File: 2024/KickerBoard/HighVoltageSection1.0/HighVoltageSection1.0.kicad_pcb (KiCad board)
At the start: 2 copper layers, 59.8 x 28.9 mm, 17 parts, among them J10 Conn_01x02_Socket, J3 Conn_01x02_Socket, J4 Conn_01x02_Socket, J6 Conn_01x02_Socket, J7 Conn_01x02_Socket, J8 Conn_01x04_Socket, J9 Conn_01x04_Socket, Q2 NMOS, Q3 NMOS

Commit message: add Kick&Sub
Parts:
- J3, J4, J6, J7: footprint Connector_AMASS:AMASS_XT30UPB-F_1x02_P5.0mm_Vertical -> Connector_Molex:Molex_SPOX_5267-02A_1x02_P2.50mm_Vertical
- moved J3 125.3 mm to (-29.6, -8.27)
- moved J6 113.2 mm to (-23.8, 10.4)
- moved Q3 111.7 mm to (24.7, -5.62)
- moved J10 111.1 mm to (-5.00, -1.00)
- moved C8 110.3 mm to (-8.63, -7.63)
- moved D3 110.3 mm to (21.1, 0.60)
- moved G*** 110.3 mm to (2.00, -5.87)
- moved J9 110.3 mm to (17.3, -12.1)
- moved R10 110.3 mm to (21.8, -4.22)
- moved R11 110.3 mm to (21.8, -6.51)
- moved J7 108.7 mm to (22.6, 9.50)
- moved J8 108.6 mm to (-20.1, -11.8)
- moved Q2 107.2 mm to (-24.7, -5.62)
- moved R9 106.9 mm to (-20.4, -5.67)
- moved R8 106.5 mm to (-20.2, -2.87)
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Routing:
- net CHIP: track 51.0 -> 27.4 mm
- net STRAIGHT: track 23.0 -> 12.6 mm
- net GATE1: track 0.00 -> 3.10 mm
- net VOUT: vias 37 -> 27
- net OUTGND2: vias 8 -> 6
- net OUTGND1: vias 7 -> 5
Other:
- board size 59.8 x 28.9 mm -> 66 x 27.4 mm

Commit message: add Kick&Sub
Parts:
- removed J10: Conn_01x02_Socket, Connector_PinHeader_2.54mm:PinHeader_1x02_P2.54mm_Vertical
- removed J8, J9: Conn_01x04_Socket, Connector_PinHeader_2.54mm:PinHeader_2x02_P2.54mm_Vertical
- added J2: Conn_01x02_Socket, Connector_PinHeader_2.54mm:PinHeader_1x02_P2.54mm_Vertical, F.Cu at (-5.00, -0.12)
- added J3: Conn_01x02_Socket, Connector_PinHeader_2.54mm:PinHeader_1x02_P2.54mm_Vertical, F.Cu at (-20.0, -9.00)
- added J4: Conn_01x02_Socket, Connector_PinHeader_2.54mm:PinHeader_1x02_P2.54mm_Vertical, F.Cu at (20.0, -9.00)
- moved G*** 9.00 mm to (11.0, -6.00)
- moved Q2 6.58 mm to (-30.5, -2.50)
- moved Q3 6.47 mm to (30.5, -2.75)
- moved C8 6.04 mm to (-13.9, -10.5)
- moved J4 5.31 mm to (25.5, -8.00)
- moved R9 4.89 mm to (-25.0, -4.00)
- moved R8 4.88 mm to (-25.0, -2.00)
- moved J3 4.67 mm to (-25.5, -10.5), turned to -90 degrees
- moved D2 4.40 mm to (-22.0, 2.00)
- moved R11 4.03 mm to (25.0, -4.00)
- moved R10 3.86 mm to (25.0, -2.00)
- moved D3 1.64 mm to (22.0, 2.00)
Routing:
- net STRAIGHT: track 12.6 -> 17.4 mm
- net GATE1: track 3.10 -> 0.00 mm
- net CHIP: track 27.4 -> 30.0 mm
- net VOUT: vias 27 -> 7
- net OUTGND2: vias 6 -> 1
- net OUTGND1: vias 5 -> 1
- net GNDPWR: vias 35 -> 25
- added copper zone on F.Cu, net GATE1
- added copper zone on F.Cu, net GATE2

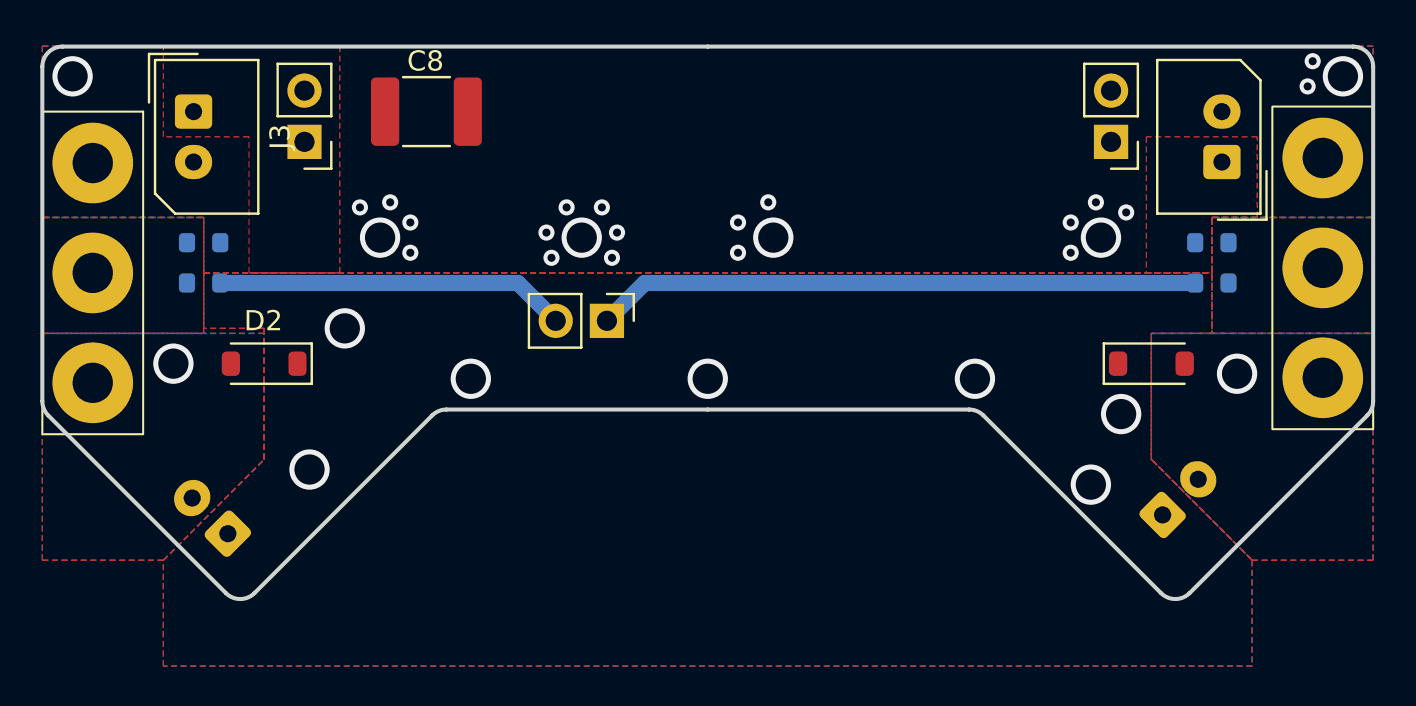
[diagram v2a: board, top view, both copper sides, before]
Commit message: add Sub&dcdc
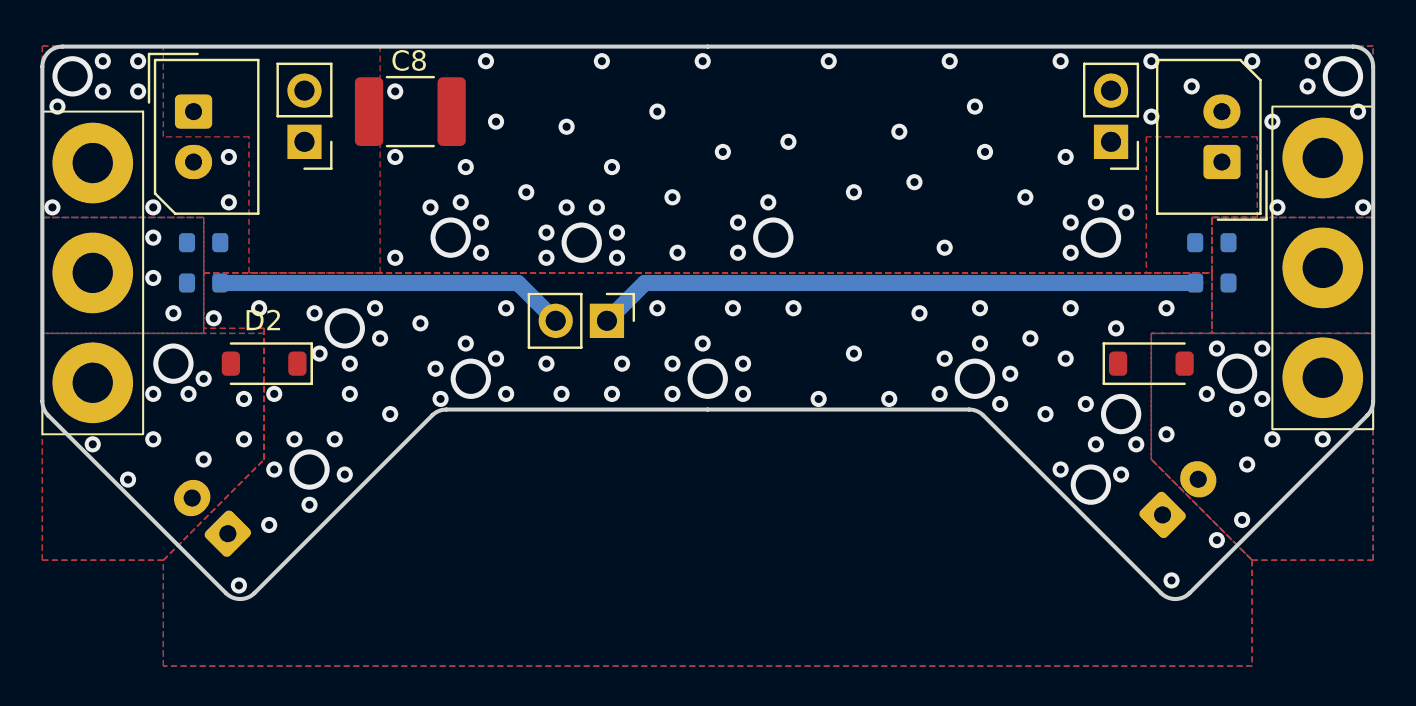
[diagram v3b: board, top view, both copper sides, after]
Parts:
- moved C8 0.80 mm to (-14.8, -10.5)
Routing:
- net VOUT: vias 7 -> 66
- net OUTGND2: vias 1 -> 11
- net OUTGND1: vias 1 -> 10
- net GNDPWR: vias 25 -> 69
- net GATE1: vias 0 -> 3

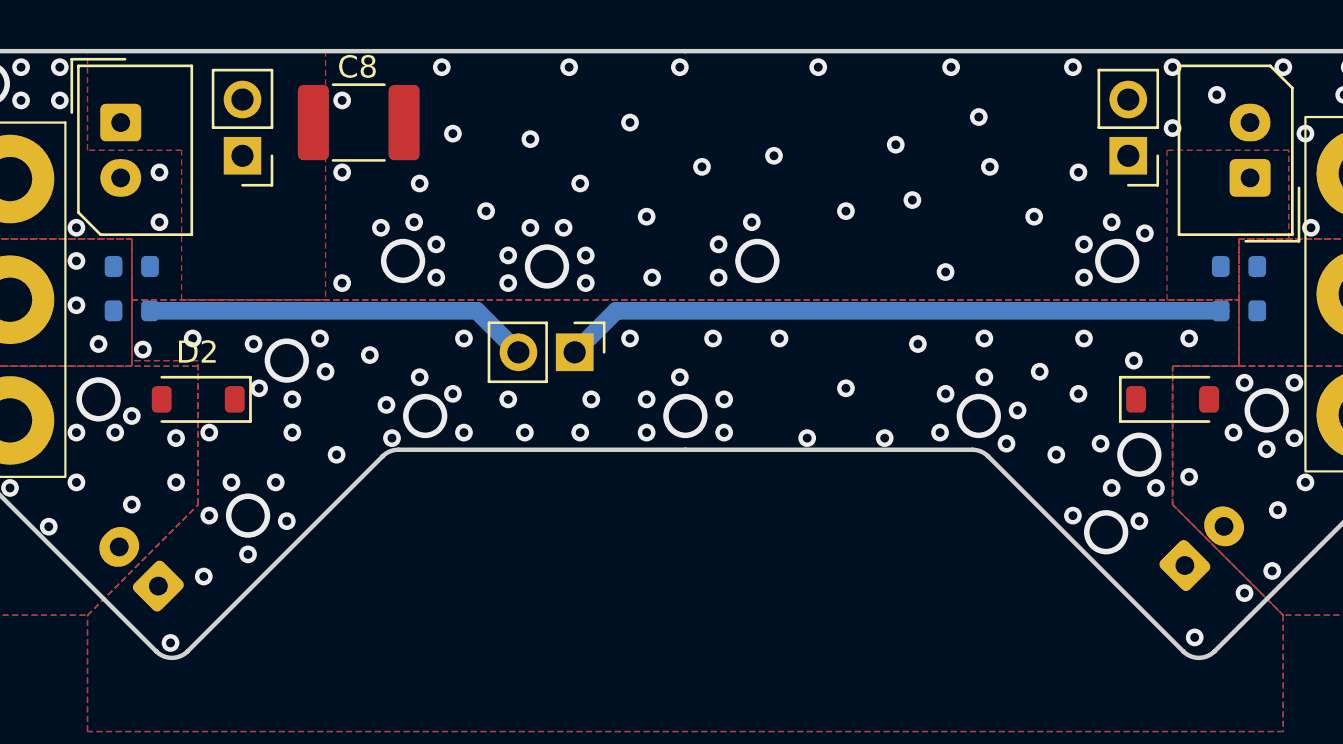
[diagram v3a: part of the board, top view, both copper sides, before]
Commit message: improved schematic readability
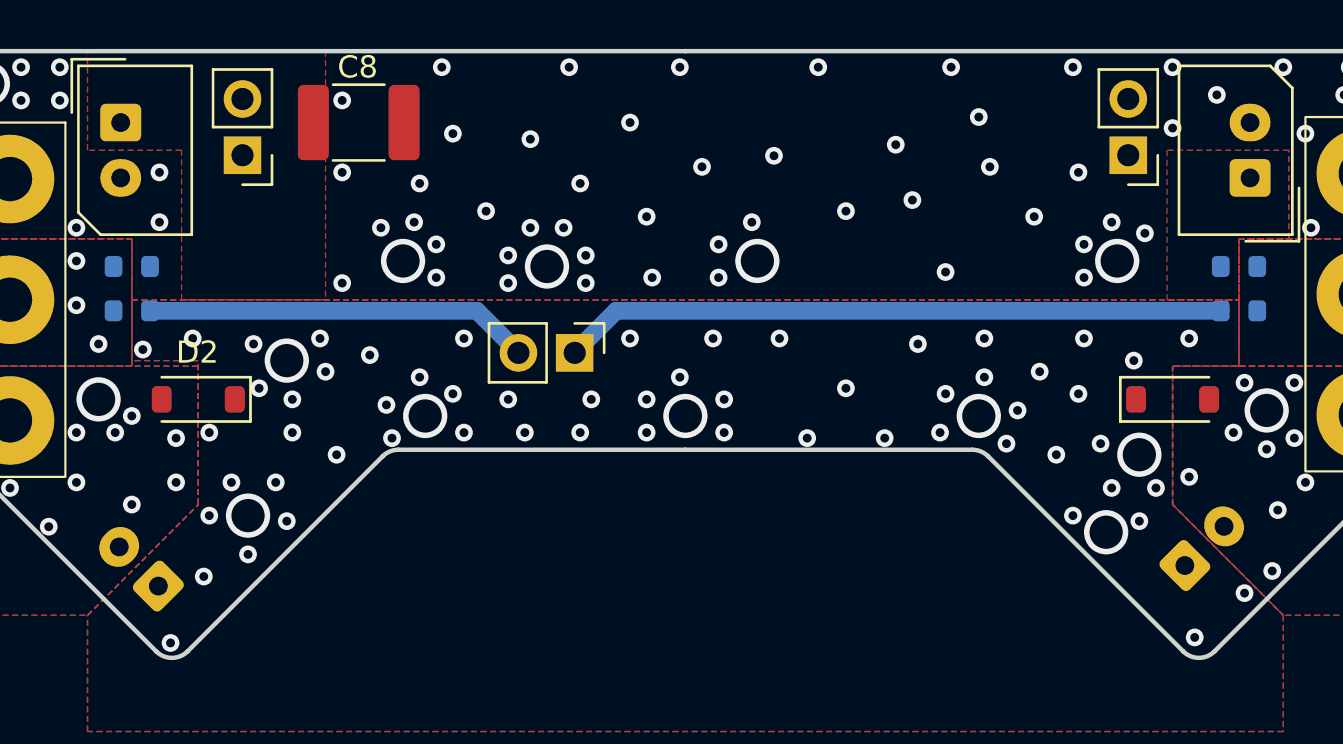
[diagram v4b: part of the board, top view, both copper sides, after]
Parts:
- removed the J3 at (-25.5, -10.5)
- removed the J4 at (20.0, -9.00)
- added J1: Conn_01x02_Socket, Connector_PinHeader_2.54mm:PinHeader_1x02_P2.54mm_Vertical, F.Cu at (-20.0, -9.03)
- added J10: Conn_01x02_Socket, Connector_PinHeader_2.54mm:PinHeader_1x02_P2.54mm_Vertical, F.Cu at (-5.00, -0.10)
- J3: footprint Connector_PinHeader_2.54mm:PinHeader_1x02_P2.54mm_Vertical -> Connector_Molex:Molex_SPOX_5267-02A_1x02_P2.50mm_Vertical
- moved J2 26.5 mm to (20.0, -9.03), turned to 180 degrees
- moved J3 5.70 mm to (-25.5, -10.5), turned to -90 degrees
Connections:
- net OUTGND1 renamed GND1
- net OUTGND2 renamed GND2
- J2 pad 1: CHIP -> GNDPWR
- J2 pad 2: STRAIGHT -> GNDPWR
- J3 pad 2: VOUT -> GNDPWR
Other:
- board text added: "BoostCircuitHighVoltageSection2.0 20240411 KotaroOCHIISHI"
- board text removed: "BoostCircuitHighVoltageSection1.0 20240321 KotaroOCHIISHI"
